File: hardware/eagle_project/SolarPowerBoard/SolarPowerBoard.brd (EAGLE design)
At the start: 68.8 x 53.6 mm, 77 parts, among them IC1 BQ29700DSET, IC3 TPS63031DSKT, J2 105017-0001, J5 XG8S-0331, K1 G6E-134P-US_DC5, Q3 FDN302P, U4 MCP73831T-2ACI/OT

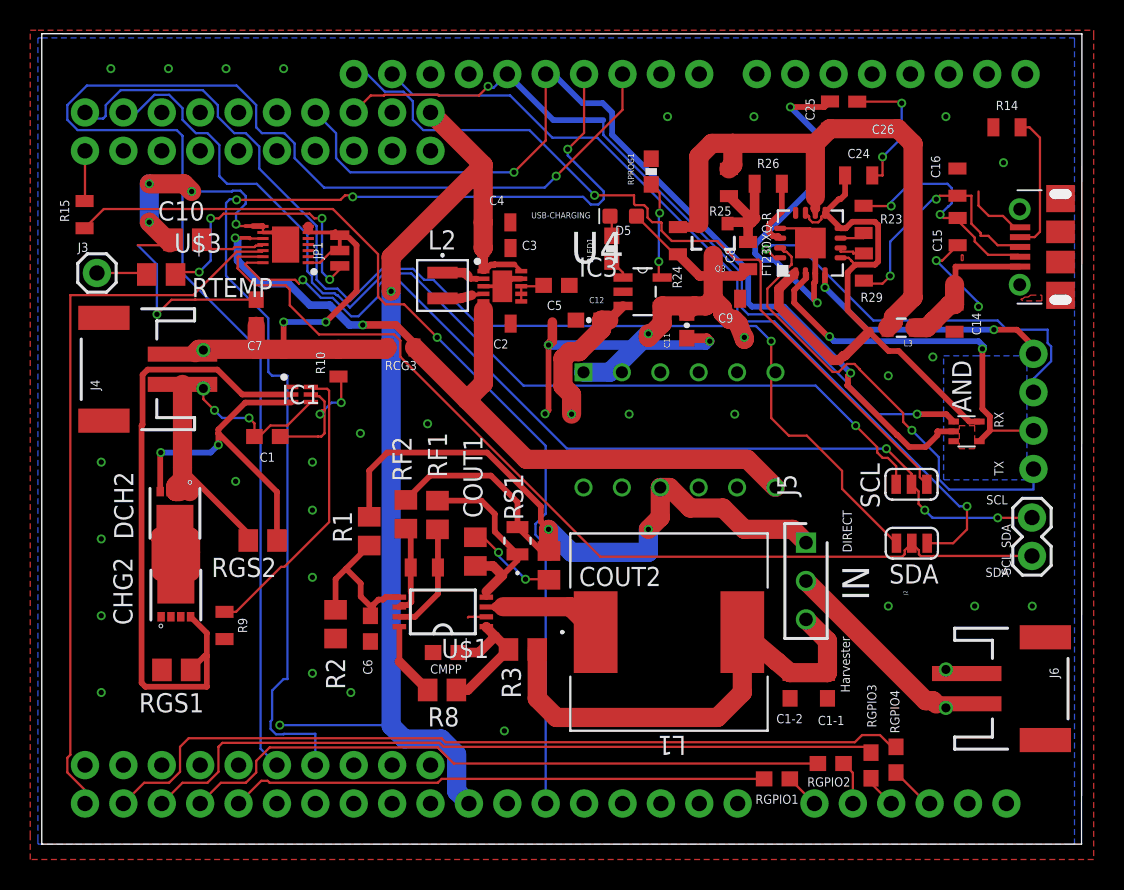
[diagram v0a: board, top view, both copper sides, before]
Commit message: First check. Few things to modify:
- rearrange kelvin connections on sensing resistor (and routing around the fuel gauge)
- add LED on CBUS1 and CBUS2 of the FTDI chip (see powerDevPack project), or remove the CBUS1 and CBUS2 connections
- edit the JST connector footprint and increase holes size (see J5 footprint as reference)
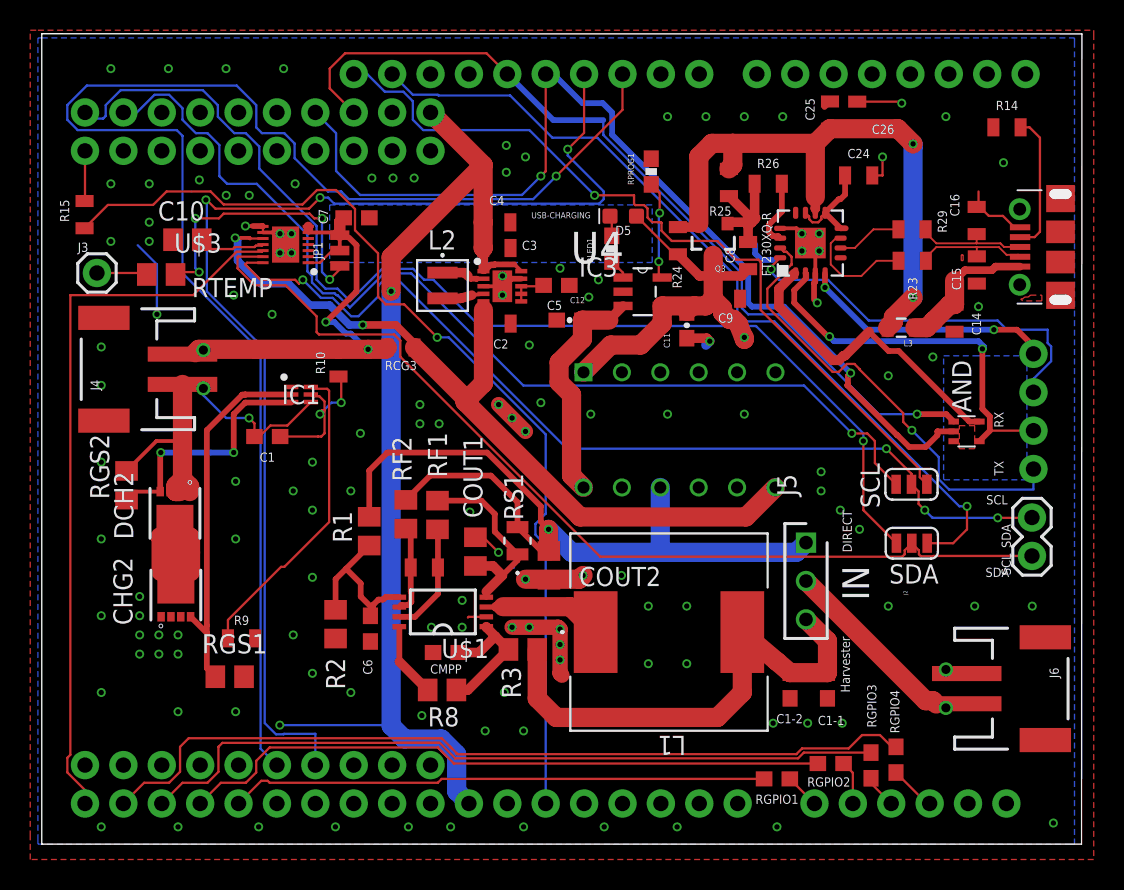
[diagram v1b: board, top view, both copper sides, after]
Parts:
- moved RGS2 9.72 mm to (4.85, 23.2), turned to 90 degrees
- moved C7 9.12 mm to (20.1, 40.9), turned to 180 degrees
- moved R23 4.23 mm to (56.8, 38.1), turned to 0 degrees
- moved R29 4.05 mm to (56.8, 40.2), turned to 180 degrees
- moved RGS1 3.56 mm to (11.7, 10.6), turned to 180 degrees
- moved C16 2.84 mm to (61.1, 40.8)
- moved C15 2.84 mm to (61.1, 37.5)
- moved R9 1.41 mm to (12.5, 13.1), turned to 0 degrees
- moved C12 1.27 mm to (34.2, 34.2)
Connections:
- net N$31 renamed USBDR_N
- net N$32 renamed USBDR_P
- net GND: no longer CHG2.9, DCH2.9
- net N$14: now also CHG2.9, DCH2.9
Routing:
- net GND: track 110.0 -> 46.3 mm, vias 44 -> 129
- net N$15: track 42.0 -> 24.8 mm
- net VCCIO_FTDI: track 40.3 -> 27.5 mm
- net USBD_P: track 16.8 -> 7.99 mm, vias 2 -> 0
- net USBD_N: track 15.5 -> 7.78 mm, vias 2 -> 0
- net N$20: track 9.68 -> 15.5 mm, vias 1 -> 0
- net USBDR_N: track 1.86 -> 7.42 mm
- net N$22: track 21.9 -> 16.6 mm
- net PO.25(RX)-DIO3(TX): track 52.4 -> 57.3 mm, vias 2 -> 1
- net N$40: track 63.4 -> 66.5 mm
- net PO.24(TX)-DIO2(RX): track 63.8 -> 66.7 mm
- net USBDR_P: track 1.90 -> 4.34 mm
- net N$19: track 25.5 -> 23.2 mm, vias 2 -> 1
- net POWER_INPUT: track 51.8 -> 53.6 mm
- net PACK+: track 27.7 -> 26.5 mm
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- added copper zone on layer 16, net GROUND_CUT

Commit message: Fixed library link. Several small problems fixed.
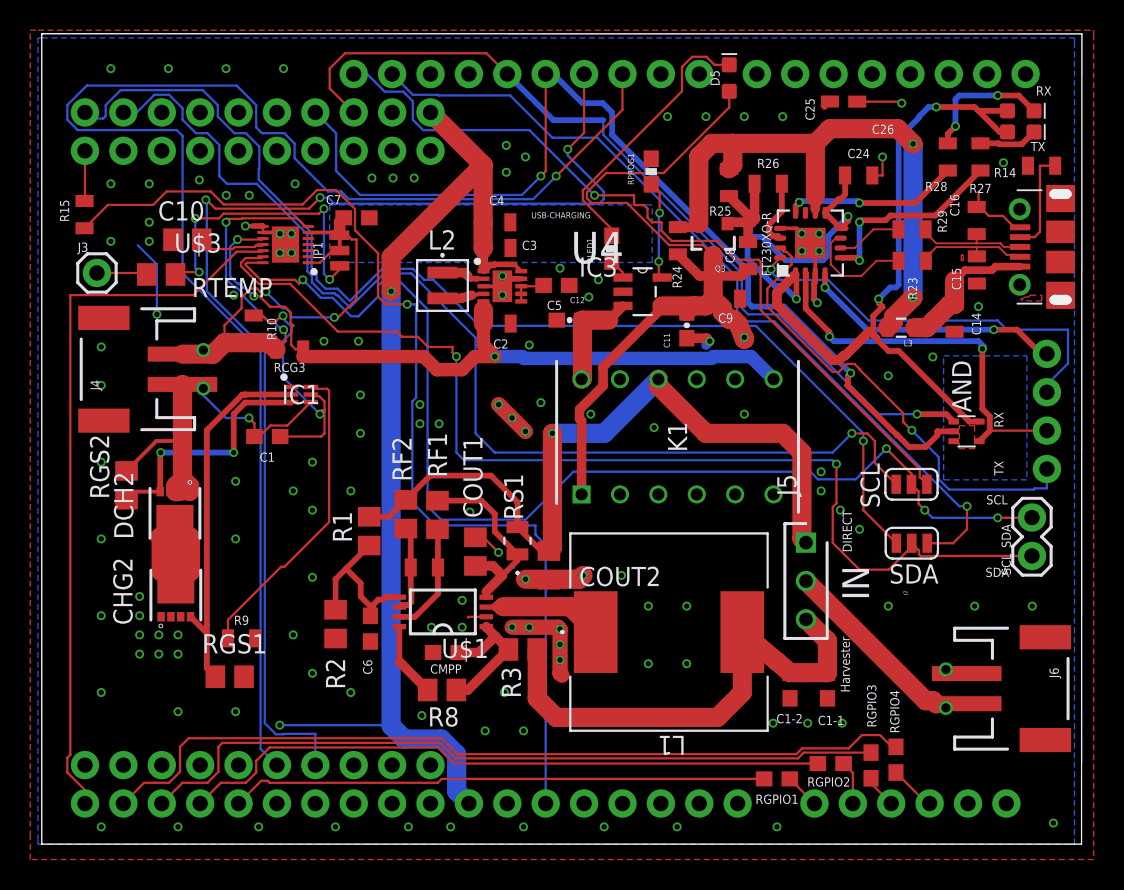
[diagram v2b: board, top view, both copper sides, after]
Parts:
- added R27, R28: 470, SparkFun-Resistors:0805
- added RX: ORANGE, SparkFun-LED:LED-0603
- added TX: YELLOW, SparkFun-LED:LED-0603
- AND: value 74AHC1G08DCK -> 74XX-LITTLE-DE_74AHC1G08DCK; device 74xx-little-de:SC70-5 -> SolarPowerBoard:74XX-LITTLE-DE_SC70-5
- C1, C1-1, C1-2, C5, C6, C7, CMPP: device SparkFun-Capacitors:0603 -> SolarPowerBoard:SPARKFUN-CAPACITORS_0603
- C10, COUT1, COUT2: device resistor:C0805 -> SolarPowerBoard:RESISTOR_C0805
- C11, C12: device SparkFun-Capacitors:0603-CAP -> SolarPowerBoard:SPARKFUN-CAPACITORS_0603-CAP
- C14: value 10uF -> 10nF; device SparkFun-Capacitors:0805 -> SolarPowerBoard:SPARKFUN-CAPACITORS_0805:1
- C15, C16: value 10uF -> 47pF; device SparkFun-Capacitors:0805 -> SolarPowerBoard:SPARKFUN-CAPACITORS_0805:1
- C2, C4, CF: device SparkFun-Capacitors:0805 -> SolarPowerBoard:SPARKFUN-CAPACITORS_0805
- C24, C26, C8, C9: value 10uF -> 100nF; device SparkFun-Capacitors:0805 -> SolarPowerBoard:SPARKFUN-CAPACITORS_0805:1
- C25: value 10uF -> 4.7uF; device SparkFun-Capacitors:0805 -> SolarPowerBoard:SPARKFUN-CAPACITORS_0805:1
- C3: value 10UF -> 10uF; device SparkFun-Capacitors:0805 -> SolarPowerBoard:SPARKFUN-CAPACITORS_0805
- CHG2, DCH2: value CSD16406Q3 -> SOLARCOMPONENTS_CSD16406Q3; device SolarComponents:CSD16327 -> SolarPowerBoard:SOLARCOMPONENTS_CSD16327
- D5: device SparkFun-LED:LED-0603 -> SolarPowerBoard:SPARKFUN-LED_LED-0603
- FT230XQ-R: device FT230XQ:QFN16 -> SolarPowerBoard:FT230XQ_QFN16
- IC1: value BQ29700DSET -> BQ29700DSET_BQ29700DSET; device BQ29700DSET:SON50P150X150X80-6N -> SolarPowerBoard:BQ29700DSET_SON50P150X150X80-6N
- IC3: value TPS63031DSKT -> TPS63031DSKT_TPS63031DSKT; device TPS63031DSKT:SON50P250X250X80-11N -> SolarPowerBoard:TPS63031DSKT_SON50P250X250X80-11N
- J2: value 105017-0001 -> 105017-0001_105017-0001; device 105017-0001:MOLEX_105017-0001 -> SolarPowerBoard:105017-0001_MOLEX_105017-0001
- J3: device SparkFun-Connectors:1X01 -> SolarPowerBoard:SPARKFUN-CONNECTORS_1X01
- J4, J6: device SolarComponents:JST-2-SMD -> SolarPowerBoard:SOLARCOMPONENTS_JST-2-SMD
- J5: value XG8S-0331 -> XG8S-0331_XG8S-0331; device XG8S-0331:HDRV3W70P0X254_1X3_760X280X680 -> SolarPowerBoard:XG8S-0331_HDRV3W70P0X254_1X3_760X280X680
- JP1: value JUMPER-SMT_3_1-NC_TRACE_NO-SILK -> SPARKFUN-JUMPERS_JUMPER-SMT_3_1-NC_TRACE_NO-SILK; device SparkFun-Jumpers:SMT-JUMPER_3_1-NC_TRACE_NO-SILK -> SolarPowerBoard:SPARKFUN-JUMPERS_SMT-JUMPER_3_1-NC_TRACE_NO-SILK
- K1: value G6E-134P-US_DC5 -> G6E-134P-US_DC5_G6E-134P-US_DC5; device G6E-134P-US_DC5:DIP762W60P254L1595H800Q12N -> SolarPowerBoard:G6E-134P-US_DC5_DIP762W60P254L1595H800Q12N
- L1: value SRR1280-270M -> SOLARPOWERBOARD_SRR1280-270M; device SolarPowerBoard:IND_BOURNS_SRR1280 -> SolarPowerBoard:SOLARPOWERBOARD_IND_BOURNS_SRR1280
- L2: value SRN3010-470M -> SRN3010-470M_SRN3010-470M; device SRN3010-470M:IND_BOURNS_SRN3010 -> SolarPowerBoard:SRN3010-470M_IND_BOURNS_SRN3010
- L3: device davide:0805 -> SolarPowerBoard:DAVIDE_0805:1
- Q3: value FDN302P -> DAVIDE_FDN302P; device davide:SOT23-3 -> SolarPowerBoard:DAVIDE_SOT23-3
- R1, R2, R3, R8, RF1, RF2, RGS1, RGS2, RTEMP: device resistor:R0805 -> SolarPowerBoard:RESISTOR_R0805
- R10: value 330 -> (none); device SparkFun-Resistors:0805 -> SolarPowerBoard:SPARKFUN-RESISTORS_0805:2
- R14, R25: value 0.3 -> 100k; device SparkFun-Resistors:0805 -> SolarPowerBoard:SPARKFUN-RESISTORS_0805:1
- R15: device SparkFun-Resistors:0805 -> SolarPowerBoard:SPARKFUN-RESISTORS_0805:1
- R23, R29: value 0.3 -> 27; device SparkFun-Resistors:0805 -> SolarPowerBoard:SPARKFUN-RESISTORS_0805:1
- R24: value 0.3 -> DNM; device SparkFun-Resistors:0805 -> SolarPowerBoard:SPARKFUN-RESISTORS_0805:1
- R26: value 0.3 -> 1k; device SparkFun-Resistors:0805 -> SolarPowerBoard:SPARKFUN-RESISTORS_0805:1
- R9: value 2.2k -> (none); device SparkFun-Resistors:0805 -> SolarPowerBoard:SPARKFUN-RESISTORS_0805:2
- RB2: value CC2650LAUNCHPAD -> POWERSOL_CC2650LAUNCHPAD; device powersol:SEPS_RB -> SolarPowerBoard:POWERSOL_SEPS_RB
- RCG3: value 1mOhm -> (none); device SparkFun-Resistors:0805 -> SolarPowerBoard:SPARKFUN-RESISTORS_0805:2
- RGPIO1, RGPIO2, RGPIO3, RGPIO4: device SparkFun-Resistors:0603 -> SolarPowerBoard:SPARKFUN-RESISTORS_0603:2
- RLED1, RPROG1: device SparkFun-Passives:0603-RES -> SolarPowerBoard:SPARKFUN-PASSIVES_0603-RES
- RS1: value RL1220T-R010-J -> RL1220T-R010-J_RL1220T-R010-J; device RL1220T-R010-J:RES_1220 -> SolarPowerBoard:RL1220T-R010-J_RES_1220
- RX_TX: device SparkFun-Connectors:1X04 -> SolarPowerBoard:SPARKFUN-CONNECTORS_1X04
- SCL, SDA: value JUMPER-SMT_3_0_SILK -> POWERSOL_JUMPER-SMT_3_0_SILK; device powersol:SMT-JUMPER_3_0_NC_TRACE_SILK -> SolarPowerBoard:POWERSOL_SMT-JUMPER_3_0_NC_TRACE_SILK
- SCL_SDA: device SparkFun-Connectors:1X02 -> SolarPowerBoard:SPARKFUN-CONNECTORS_1X02
- U$1: value SVP1040 -> SOLARCOMPONENTS_SVP1040; device SolarComponents:TSSOP-8 -> SolarPowerBoard:SOLARCOMPONENTS_TSSOP-8
- U$2: value PCA10040NORDIC -> POWERSOL_PCA10040NORDIC; device powersol:SEPS_BB -> SolarPowerBoard:POWERSOL_SEPS_BB
- U$3: value MAX17260 -> SOLARCOMPONENTS_MAX17260; device SolarComponents:SON40P300X300X80-15N -> SolarPowerBoard:SOLARCOMPONENTS_SON40P300X300X80-15N
- U4: value MCP73831T-2ACI/OT -> MCP73831T-2ACI_OT_MCP73831T-2ACI/OT; device MCP73831T-2ACI_OT:SOT95P280X145-5N -> SolarPowerBoard:MCP73831T-2ACI_OT_SOT95P280X145-5N
- moved D5 11.5 mm to (44.7, 50.2), turned to 90 degrees
- moved RCG3 7.37 mm to (15.6, 32.2)
- moved R10 6.04 mm to (13.3, 33.6), turned to 270 degrees
- moved R14 3.42 mm to (65.4, 44.4)
- moved RX_TX 0.89 mm to (65.7, 24.3)
- moved K1 0.48 mm to (41.3, 26.4), flipped to the top, turned to 90 degrees
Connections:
- new net N$31: FT230XQ-R.12, R28.1
- new net N$32: R28.2, RX.C
- new net N$42: R27.2, TX.C
- new net N$43: FT230XQ-R.5, R27.1
- net VCCIO_FTDI: now also RX.A, TX.A; no longer FT230XQ-R.11, FT230XQ-R.5
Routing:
- net VCCIO_FTDI: track 27.5 -> 68.3 mm, vias 0 -> 4
- net VDD_CHARGER: track 27.8 -> 54.2 mm
- net PACK+: track 26.5 -> 44.3 mm, vias 2 -> 4
- net N$9: track 1.35 -> 18.3 mm
- net N$43: track 0.00 -> 13.3 mm, vias 0 -> 2
- net SCL_FG: track 63.8 -> 75.8 mm
- net N$31: track 0.00 -> 11.8 mm, vias 0 -> 2
- net N$32: track 0.00 -> 8.97 mm, vias 0 -> 2
- net N$20: track 15.5 -> 7.01 mm
- net N$24: track 10.4 -> 17.1 mm
- net SDA_FG: track 65.2 -> 71.2 mm, vias 0 -> 2
- net N$37: track 68.3 -> 73.1 mm
- net SOLAR_OUTPUT: track 55.0 -> 50.3 mm
- net N$42: track 0.00 -> 3.91 mm
- net N$40: track 66.5 -> 70.0 mm
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
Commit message: Added Nordic TX pin pull up resistor
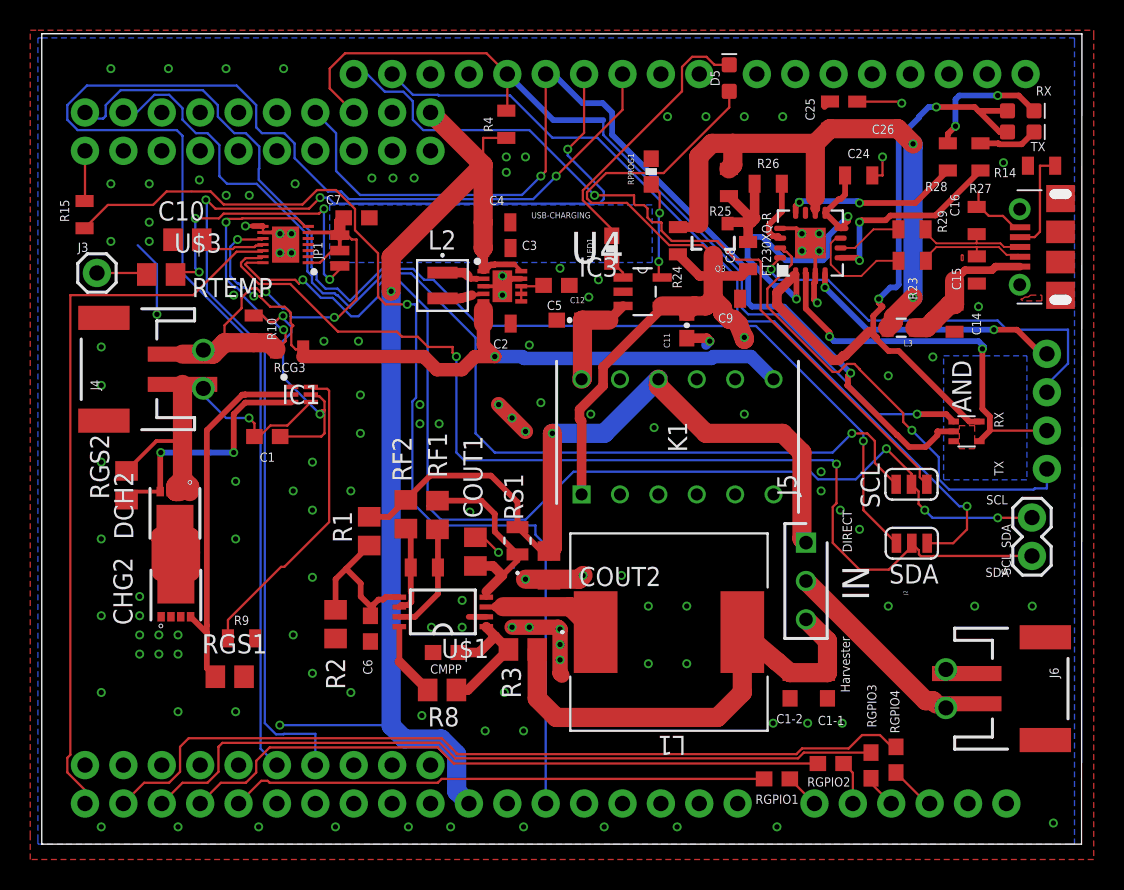
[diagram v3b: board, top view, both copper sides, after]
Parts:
- added R4: 100k, SolarPowerBoard:SPARKFUN-RESISTORS_0805:1
- R15: value 0.3 -> 0
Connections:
- net PO.25(RX)-DIO3(TX): now also R4.2
- net VDD: now also R4.1
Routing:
- net VDD: track 70.8 -> 74.2 mm
- net PO.25(RX)-DIO3(TX): track 57.3 -> 59.7 mm
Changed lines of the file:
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@@
 <attribute name="PROD_ID" value="RES-11622" x="133.964" y="-43.254" size="1.778" layer="27" display="off"/>
 </element>
-<element name="R15" library="SolarPowerBoard" package="SPARKFUN-RESISTORS_0805:1" value="0.3" x="2.07" y="41.14" rot="R90">
+<element name="R15" library="SolarPowerBoard" package="SPARKFUN-RESISTORS_0805:1" value="0" x="2.07" y="41.14" rot="R90">
 <attribute name="MF" value="" x="89.7" y="113.53" size="1.778" layer="27" rot="R90" display="off"/>
 <attribute name="MPN" value="RLP73N2AR30JTD" x="89.7" y="113.53" size="1.778" layer="27" rot="R90" display="off"/>
@@
 <attribute name="NAME" x="58.42" y="43.307" size="0.6096" layer="25" font="vector" ratio="20" rot="R180" align="bottom-center"/>
 <attribute name="PROD_ID" value="RES-11622" x="70.612" y="42.418" size="1.778" layer="27" rot="R90" display="off"/>
+</element>
+<element name="R4" library="SolarPowerBoard" package="SPARKFUN-RESISTORS_0805:1" value="100k" x="29.972" y="47.117" rot="R90">
+<attribute name="MF" value="" x="29.972" y="47.117" size="1.778" layer="27" rot="R90" display="off"/>
+<attribute name="MPN" value="RLP73N2AR30JTD" x="29.972" y="47.117" size="1.778" layer="27" rot="R90" display="off"/>
+<attribute name="NAME" x="29.083" y="47.117" size="0.6096" layer="25" font="vector" ratio="20" rot="R90" align="bottom-center"/>
+<attribute name="OC_NEWARK" value="43AC3996" x="29.972" y="47.117" size="1.778" layer="27" rot="R90" display="off"/>
+<attribute name="PROD_ID" value="RES-11622" x="29.972" y="47.117" size="1.778" layer="27" rot="R90" display="off"/>
+<attribute name="VALUE" x="32.131" y="47.117" size="0.6096" layer="27" font="vector" ratio="20" rot="R90" align="top-center"/>
 </element>
 </elements>
@@
 <wire x1="61.893" y1="41.0564" x2="61.214" y2="41.7354" width="0.1524" layer="1"/>
 <wire x1="61.214" y1="41.7354" x2="61.214" y2="42.672" width="0.1524" layer="1"/>
-<wire x1="28.648" y1="14.531" x2="27.485" y2="14.531" width="0.1524" layer="1"/>
+<wire x1="28.648" y1="14.531" x2="27.485" y2="14.531" width="0.381" layer="1"/>
 <wire x1="27.485" y1="14.531" x2="27.432" y2="14.478" width="0.1524" layer="1"/>
 <wire x1="32.793" y1="16.981" x2="32.756" y2="17.018" width="0.1524" layer="1"/>
@@
 <via x="39.37" y="11.43" extent="1-16" drill="0.35"/>
 <via x="23.876" y="43.561" extent="1-16" drill="0.35"/>
-<via x="29.972" y="45.72" extent="1-16" drill="0.35"/>
+<via x="29.972" y="44.958" extent="1-16" drill="0.35"/>
 <via x="29.972" y="43.942" extent="1-16" drill="0.35"/>
 <via x="31.242" y="44.958" extent="1-16" drill="0.35"/>
@@
 <wire x1="28.91796875" y1="37.7929" x2="28.53506875" y2="37.41" width="0.381" layer="1"/>
 <wire x1="28.45" y1="38.93" x2="28.45" y2="37.5199" width="0.635" layer="1"/>
+<contactref element="R4" pad="1"/>
+<wire x1="29.972" y1="46.217" x2="28.44" y2="46.217" width="0.1524" layer="1"/>
+<wire x1="28.44" y1="46.217" x2="28.44" y2="44.42" width="0.1524" layer="1"/>
 <wire x1="28.45" y1="37.5199" x2="28.46" y2="37.4" width="0" layer="19" extent="1-1"/>
 </signal>
@@
 <wire x1="18.288" y1="49.492" x2="19.8788" y2="47.9012" width="0.1524" layer="1"/>
 <wire x1="18.288" y1="50.8" x2="18.288" y2="49.492" width="0.1524" layer="1"/>
+<contactref element="R4" pad="2"/>
+<wire x1="30.0388" y1="50.4412" x2="30.0388" y2="48.0838" width="0.1524" layer="1"/>
+<wire x1="30.0388" y1="48.0838" x2="29.972" y2="48.017" width="0.1524" layer="1"/>
 </signal>
 <signal name="PO.24(TX)-DIO2(RX)">
